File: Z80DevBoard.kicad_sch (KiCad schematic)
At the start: 163 parts, among them J1 Conn_01x02_Pin, J2 Conn_02x20_Top_Bottom, J3 Conn_02x10_Top_Bottom, SW1 WAIT, SW2 RESET, SW3 Z80BOOT, SW4 RPBOOT, SW5 SW_Nidec_CAS-120A1, SW6 Z80_CLOCK, U1 74HC14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

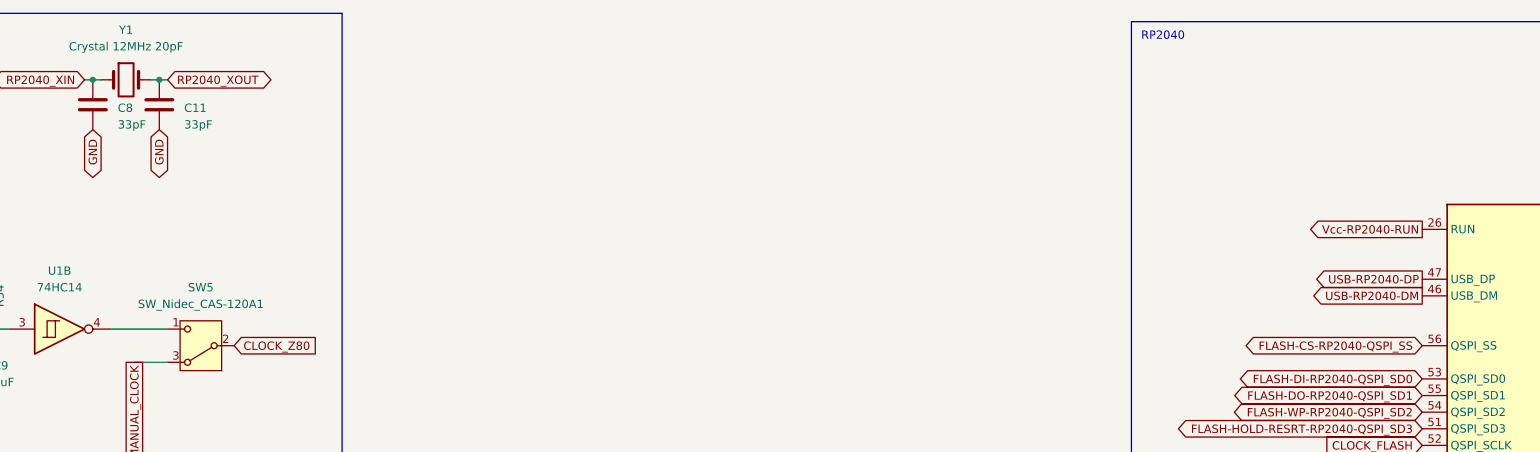
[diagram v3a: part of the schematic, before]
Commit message: Fixed the RP2040 clock capacitors. Added 2 resistors to the RP2040's XIN-XOUT.
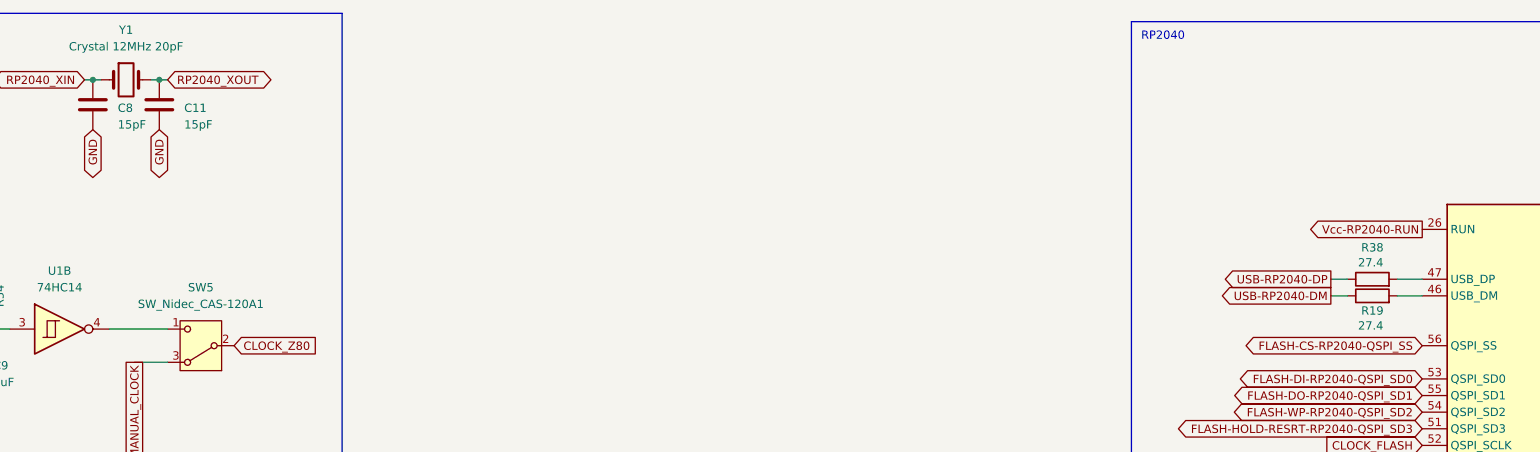
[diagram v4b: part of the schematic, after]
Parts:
- added R19, R38: 27.4, Resistor_THT:R_Axial_DIN0207_L6.3mm_D2.5mm_P10.16mm_Horizontal, symbol Device:R
- C11, C8: value 33pF -> 15pF
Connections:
- net USB-RP2040-DM: now also R19.1; no longer RP2040_1.46 (USB_DM)
- net USB-RP2040-DP: now also R38.1; no longer RP2040_1.47 (USB_DP)
- new net: R19.2, RP2040_1.46 (USB_DM)
- new net: R38.2, RP2040_1.47 (USB_DP)
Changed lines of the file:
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@@
 	(title_block
 		(title "Z80DevBoard")
-		(date "2026-03-12")
+		(date "2026-03-24")
 		(company "Gianluca Rainis")
 		(comment 1 "gianluca-rainis on GitHub")
@@
 	(wire
 		(pts
+			(xy 311.15 58.42) (xy 314.96 58.42)
+		)
+		(stroke
+			(width 0)
+			(type default)
+		)
+	)
+	(wire
+		(pts
 			(xy 458.47 43.18) (xy 452.12 43.18)
 		)
@@
 	(wire
 		(pts
+			(xy 311.15 55.88) (xy 314.96 55.88)
+		)
+		(stroke
+			(width 0)
+			(type default)
+		)
+	)
+	(wire
+		(pts
 			(xy 46.99 378.46) (xy 46.99 382.27)
 		)
@@
 	(wire
 		(pts
+			(xy 300.99 55.88) (xy 303.53 55.88)
+		)
+		(stroke
+			(width 0)
+			(type default)
+		)
+	)
+	(wire
+		(pts
 			(xy 466.09 193.04) (xy 490.22 193.04)
 		)
@@
 	(wire
 		(pts
+			(xy 300.99 58.42) (xy 303.53 58.42)
+		)
+		(stroke
+			(width 0)
+			(type default)
+		)
+	)
+	(wire
+		(pts
 			(xy 524.51 187.96) (xy 537.21 187.96)
 		)
@@
 	(global_label "USB-RP2040-DM"
 		(shape output)
-		(at 314.96 58.42 180)
+		(at 300.99 58.42 180)
 		(fields_autoplaced yes)
 		(effects
@@
 		)
 		(property "Intersheetrefs" "${INTERSHEET_REFS}"
-			(at 294.9206 58.42 0)
+			(at 280.9506 58.42 0)
 			(effects
 				(font
@@
 	(global_label "USB-RP2040-DP"
 		(shape output)
-		(at 314.96 55.88 180)
+		(at 300.99 55.88 180)
 		(fields_autoplaced yes)
 		(effects
@@
 		)
 		(property "Intersheetrefs" "${INTERSHEET_REFS}"
-			(at 295.102 55.88 0)
+			(at 281.132 55.88 0)
 			(effects
 				(font
@@
 			)
 		)
-		(property "Value" "33pF"
+		(property "Value" "15pF"
 			(at 115.57 32.258 0)
 			(effects
@@
 	)
 	(symbol
+		(lib_id "Device:R")
+		(at 307.34 58.42 90)
+		(unit 1)
+		(exclude_from_sim no)
+		(in_bom yes)
+		(on_board yes)
+		(dnp no)
+		(property "Reference" "R19"
+			(at 307.34 60.706 90)
+			(effects
+				(font
+					(size 1.27 1.27)
+				)
+			)
+		)
+		(property "Value" "27.4"
+			(at 307.086 62.992 90)
+			(effects
+				(font
+					(size 1.27 1.27)
+				)
+			)
+		)
+		(property "Footprint" "Resistor_THT:R_Axial_DIN0207_L6.3mm_D2.5mm_P10.16mm_Horizontal"
+			(at 307.34 60.198 90)
+			(effects
+				(font
+					(size 1.27 1.27)
+				)
+				(hide yes)
+			)
+		)
+		(property "Datasheet" "~"
+			(at 307.34 58.42 0)
+			(effects
+				(font
+					(size 1.27 1.27)
+				)
+				(hide yes)
+			)
+		)
+		(property "Description" "Resistor"
+			(at 307.34 58.42 0)
+			(effects
+				(font
+					(size 1.27 1.27)
+				)
+				(hide yes)
+			)
+		)
+		(pin "1"
+		)
+		(pin "2"
+		)
+		(instances
+			(project "Z80DevBoard"
+				(path "/e1d3a7c4-9081-48b0-8f4d-5da429793ec4"
+					(reference "R19")
+					(unit 1)
+				)
+			)
+		)
+	)
+	(symbol
 		(lib_id "Device:LED")
 		(at 110.49 335.28 0)
@@
 			)
 		)
-		(property "Value" "33pF"
+		(property "Value" "15pF"
 			(at 125.73 32.258 0)
 			(effects
@@
 					(unit 1)
 				)
+			)
+		)
+	)
+	(symbol
+		(lib_id "Device:R")
+		(at 307.34 55.88 90)
+		(unit 1)
+		(exclude_from_sim no)
+		(in_bom yes)
+		(on_board yes)
+		(dnp no)
+		(property "Reference" "R38"
+			(at 307.34 51.054 90)
+			(effects
+				(font
+					(size 1.27 1.27)
+				)
+			)
+		)
+		(property "Value" "27.4"
+			(at 307.086 53.34 90)
+			(effects
+				(font
+					(size 1.27 1.27)
+				)
+			)
+		)
+		(property "Footprint" "Resistor_THT:R_Axial_DIN0207_L6.3mm_D2.5mm_P10.16mm_Horizontal"
+			(at 307.34 57.658 90)
+			(effects
+				(font
+					(size 1.27 1.27)
+				)
+				(hide yes)
+			)
+		)
+		(property "Datasheet" "~"
+			(at 307.34 55.88 0)
+			(effects
+				(font
+					(size 1.27 1.27)
+				)
+				(hide yes)
+			)
+		)
+		(property "Description" "Resistor"
+			(at 307.34 55.88 0)
+			(effects
+				(font
+					(size 1.27 1.27)
+				)
+				(hide yes)
+			)
+		)
+		(pin "1"
+		)
+		(pin "2"
+		)
+		(instances
+			(project "Z80DevBoard"
+				(path "/e1d3a7c4-9081-48b0-8f4d-5da429793ec4"
+					(reference "R38")
+					(unit 1)
+				)

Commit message: Fixed some resistors.
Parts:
- R10, R11, R20, R21, R4, R7, R8, R9: value 220 -> 1k
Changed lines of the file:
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@@
 	(title_block
 		(title "Z80DevBoard")
-		(date "2026-03-24")
+		(date "2026-03-25")
 		(company "Gianluca Rainis")
 		(comment 1 "gianluca-rainis on GitHub")
@@
 			)
 		)
-		(property "Value" "220"
+		(property "Value" "1k"
 			(at 91.44 332.7399 0)
 			(effects
@@
 			)
 		)
-		(property "Value" "220"
+		(property "Value" "1k"
 			(at 66.04 332.7399 0)
 			(effects
@@
 			)
 		)
-		(property "Value" "220"
+		(property "Value" "1k"
 			(at 43.18 332.7399 0)
 			(effects
@@
 			)
 		)
-		(property "Value" "220"
+		(property "Value" "1k"
 			(at 116.84 332.7399 0)
 			(effects
@@
 			)
 		)
-		(property "Value" "220"
+		(property "Value" "1k"
 			(at 298.45 269.24 90)
 			(effects
@@
 			)
 		)
-		(property "Value" "220"
+		(property "Value" "1k"
 			(at 298.45 280.67 90)
 			(effects
@@
 			)
 		)
-		(property "Value" "220"
+		(property "Value" "1k"
 			(at 142.24 332.7399 0)
 			(effects
@@
 			)
 		)
-		(property "Value" "220"
+		(property "Value" "1k"
 			(at 167.64 332.7399 0)
 			(effects

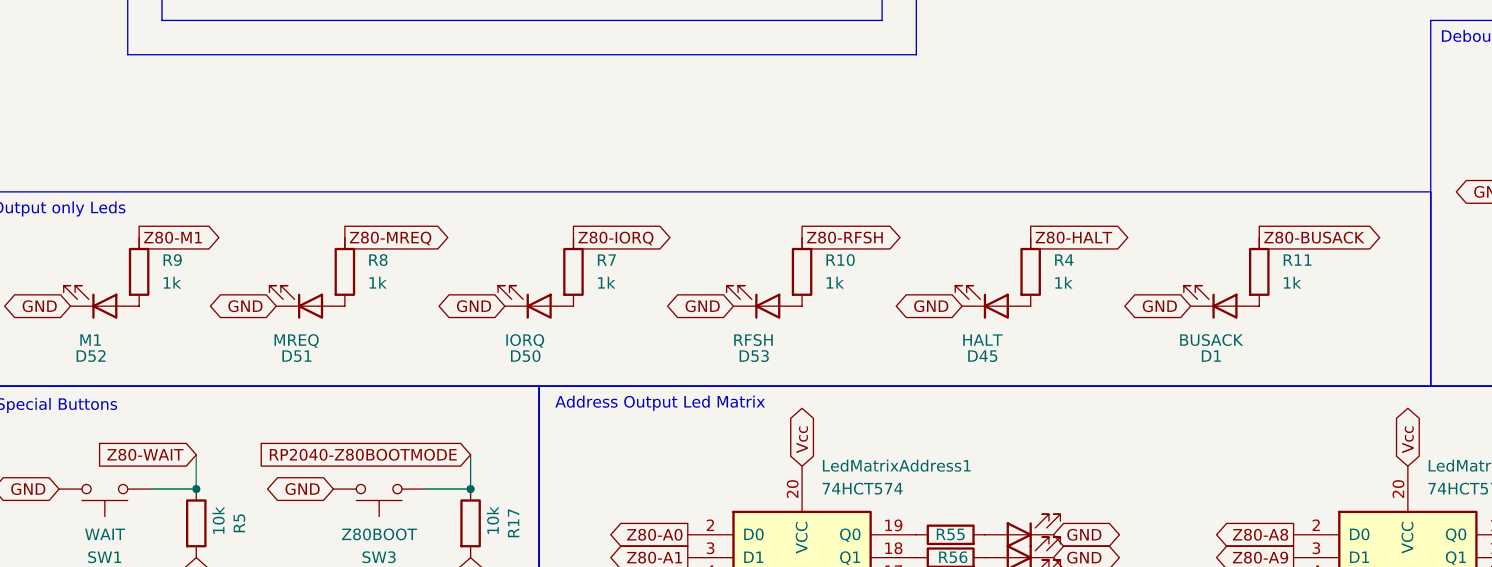
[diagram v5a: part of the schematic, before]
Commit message: Fixed some connections. Fixed some resistors values.
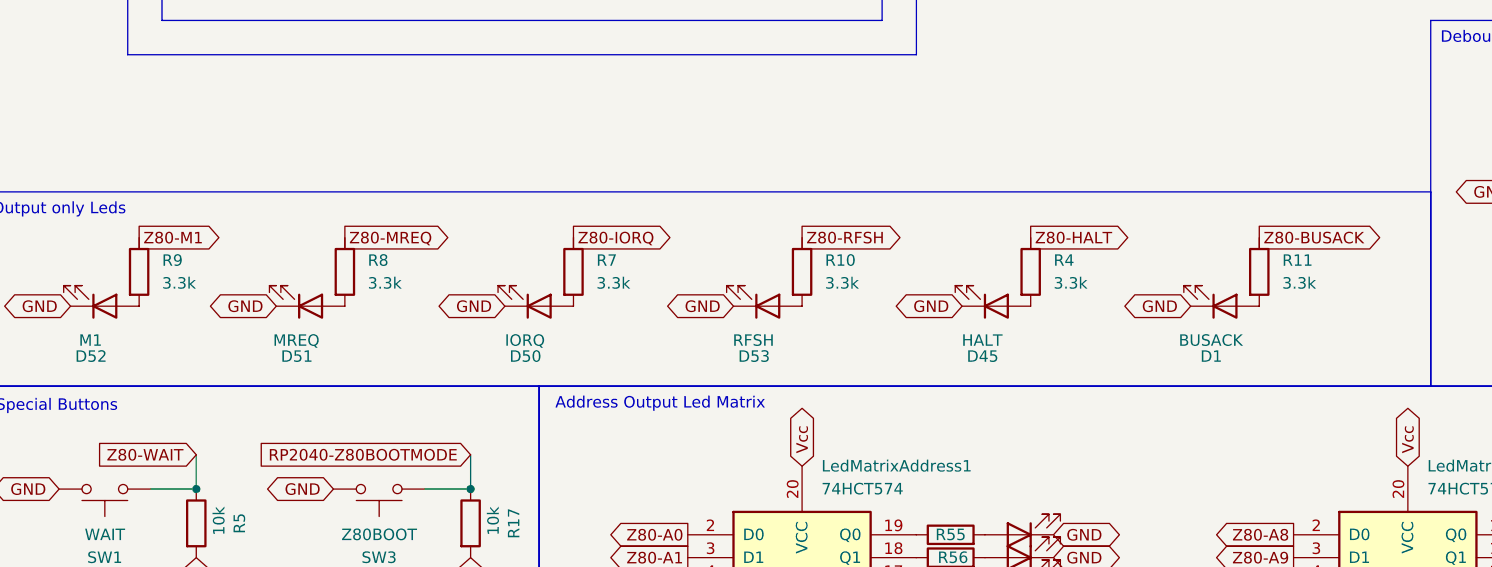
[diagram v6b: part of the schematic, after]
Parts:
- R10, R11, R4, R7, R8, R9: value 1k -> 3.3k
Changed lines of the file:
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@@
 			)
 		)
-		(property "Value" "1k"
+		(property "Value" "3.3k"
 			(at 91.44 332.7399 0)
 			(effects
@@
 			)
 		)
-		(property "Value" "1k"
+		(property "Value" "3.3k"
 			(at 66.04 332.7399 0)
 			(effects
@@
 			)
 		)
-		(property "Value" "1k"
+		(property "Value" "3.3k"
 			(at 43.18 332.7399 0)
 			(effects
@@
 			)
 		)
-		(property "Value" "1k"
+		(property "Value" "3.3k"
 			(at 116.84 332.7399 0)
 			(effects
@@
 			)
 		)
-		(property "Value" "1k"
+		(property "Value" "3.3k"
 			(at 142.24 332.7399 0)
 			(effects
@@
 			)
 		)
-		(property "Value" "1k"
+		(property "Value" "3.3k"
 			(at 167.64 332.7399 0)
 			(effects

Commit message: Added the debauncers for the Reset and the Wait buttons. Added a TXS0102DCT for the busack and busreq connections between the Z80 and the RP2040.
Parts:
- added C12, C14: 0.1uF, Capacitor_THT:CP_Radial_D4.0mm_P1.50mm, symbol Device:C
- added R39, R40: 10k, Resistor_THT:R_Axial_DIN0207_L6.3mm_D2.5mm_P10.16mm_Horizontal, symbol Device:R
- added unit 3 of U1
- added unit 4 of U1
- added U6: TXS0102DCT, Package_SO:SSOP-8_2.95x2.8mm_P0.65mm, symbol Logic_LevelTranslator:TXS0102DCT
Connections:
- net GND: now also C12.1, C14.1, U6.2 (GND)
- net RP2040-GPIO12: now also J3.1 (Pin_1); no longer J3.3 (Pin_3)
- net RP2040-GPIO13: now also J3.2 (Pin_2); no longer J3.4 (Pin_4)
- net RP2040-GPIO14: now also J3.3 (Pin_3); no longer J3.5 (Pin_5)
- net RP2040-GPIO15: now also J3.4 (Pin_4); no longer J3.6 (Pin_6)
- net RP2040-GPIO16: now also J3.5 (Pin_5); no longer J3.7 (Pin_7)
- net RP2040-GPIO17: now also J3.6 (Pin_6); no longer J3.8 (Pin_8)
- net RP2040-GPIO18: now also J3.7 (Pin_7); no longer J3.9 (Pin_9)
- net RP2040-GPIO19: now also J3.8 (Pin_8); no longer J3.10 (Pin_10)
- net RP2040-GPIO20: now also J3.9 (Pin_9); no longer J3.11 (Pin_11)
- net RP2040-GPIO21: now also J3.10 (Pin_10); no longer J3.12 (Pin_12)
- net RP2040-GPIO22: now also J3.11 (Pin_11); no longer J3.13 (Pin_13)
- net RP2040-GPIO23: now also J3.12 (Pin_12); no longer J3.14 (Pin_14)
- net RP2040-GPIO24: now also J3.13 (Pin_13); no longer J3.15 (Pin_15)
- net RP2040-GPIO25: now also J3.14 (Pin_14); no longer J3.16 (Pin_16)
- net RP2040-GPIO26-ADC0: now also J3.15 (Pin_15); no longer J3.17 (Pin_17)
- net RP2040-GPIO27-ADC1: now also J3.16 (Pin_16); no longer J3.18 (Pin_18)
- net Vcc: now also U6.7 (VCCB)
- net Vdd_3v3: now also U6.3 (VCCA), U6.6 (OE)
- net Z80-BUSACK: now also U6.1 (B2)
- net Z80-BUSREQ: now also U6.8 (B1)
- net Z80-RESET: now also U1.8; no longer R6.1, SW2.2
- net Z80-WAIT: now also U1.6; no longer R5.1, SW1.2
- net RP2040-GPIO28-ADC2: now reaches RP2040_1.40 (GPIO28_ADC2)
- net RP2040-GPIO28-ADC2: now also J3.17 (Pin_17)
- net RP2040-GPIO29-ADC3: now reaches RP2040_1.41 (GPIO29_ADC3)
- net RP2040-GPIO29-ADC3: now also J3.18 (Pin_18)
- net RP2040-GPIO10 renamed RP2040-GPIO10-BUSREQ
- net RP2040-GPIO10-BUSREQ: now also U6.5 (A1); no longer J3.1 (Pin_1)
- net RP2040-GPIO11 renamed RP2040-GPIO11-BUSACK
- net RP2040-GPIO11-BUSACK: now also U6.4 (A2); no longer J3.2 (Pin_2)
- new net: C12.2, R39.2, U1.5
- new net: R39.1, R5.1, SW1.2
- new net: R40.1, R6.1, SW2.2
- new net: C14.2, R40.2, U1.9
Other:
- note added: "RP2040 Z80 Connections"
- moved on the sheet: C7, Flash1, R17, R18, R5, R6, RAM1, RAM2, SW1, SW2, SW3, SW4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

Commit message: Fixed the capacitors sizes.
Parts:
- C1, C10, C11, C12, C13, C14, C2, C3, C4, C5, C6, C7, C8, C9: footprint Capacitor_THT:CP_Radial_D4.0mm_P1.50mm -> Capacitor_THT:CP_Radial_D4.0mm_P2.00mm
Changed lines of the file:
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@@
 			)
 		)
-		(property "Footprint" "Capacitor_THT:CP_Radial_D4.0mm_P1.50mm"
+		(property "Footprint" "Capacitor_THT:CP_Radial_D4.0mm_P2.00mm"
 			(at 221.2848 287.02 0)
 			(effects
@@
 			)
 		)
-		(property "Footprint" "Capacitor_THT:CP_Radial_D4.0mm_P1.50mm"
+		(property "Footprint" "Capacitor_THT:CP_Radial_D4.0mm_P2.00mm"
 			(at 110.7948 25.4 0)
 			(effects
@@
 			)
 		)
-		(property "Footprint" "Capacitor_THT:CP_Radial_D4.0mm_P1.50mm"
+		(property "Footprint" "Capacitor_THT:CP_Radial_D4.0mm_P2.00mm"
 			(at 20.6248 72.39 0)
 			(effects
@@
 			)
 		)
-		(property "Footprint" "Capacitor_THT:CP_Radial_D4.0mm_P1.50mm"
+		(property "Footprint" "Capacitor_THT:CP_Radial_D4.0mm_P2.00mm"
 			(at 43.4848 31.75 0)
 			(effects
@@
 			)
 		)
-		(property "Footprint" "Capacitor_THT:CP_Radial_D4.0mm_P1.50mm"
+		(property "Footprint" "Capacitor_THT:CP_Radial_D4.0mm_P2.00mm"
 			(at 80.3148 261.62 0)
 			(effects
@@
 			)
 		)
-		(property "Footprint" "Capacitor_THT:CP_Radial_D4.0mm_P1.50mm"
+		(property "Footprint" "Capacitor_THT:CP_Radial_D4.0mm_P2.00mm"
 			(at 71.4248 72.39 0)
 			(effects
@@
 			)
 		)
-		(property "Footprint" "Capacitor_THT:CP_Radial_D4.0mm_P1.50mm"
+		(property "Footprint" "Capacitor_THT:CP_Radial_D4.0mm_P2.00mm"
 			(at 66.3448 31.75 0)
 			(effects
@@
 			)
 		)
-		(property "Footprint" "Capacitor_THT:CP_Radial_D4.0mm_P1.50mm"
+		(property "Footprint" "Capacitor_THT:CP_Radial_D4.0mm_P2.00mm"
 			(at 218.7448 322.58 0)
 			(effects
@@
 			)
 		)
-		(property "Footprint" "Capacitor_THT:CP_Radial_D4.0mm_P1.50mm"
+		(property "Footprint" "Capacitor_THT:CP_Radial_D4.0mm_P2.00mm"
 			(at 91.7448 64.77 0)
 			(effects
@@
 			)
 		)
-		(property "Footprint" "Capacitor_THT:CP_Radial_D4.0mm_P1.50mm"
+		(property "Footprint" "Capacitor_THT:CP_Radial_D4.0mm_P2.00mm"
 			(at 221.2848 252.73 0)
 			(effects
@@
 			)
 		)
-		(property "Footprint" "Capacitor_THT:CP_Radial_D4.0mm_P1.50mm"
+		(property "Footprint" "Capacitor_THT:CP_Radial_D4.0mm_P2.00mm"
 			(at 32.0548 72.39 0)
 			(effects
@@
 			)
 		)
-		(property "Footprint" "Capacitor_THT:CP_Radial_D4.0mm_P1.50mm"
+		(property "Footprint" "Capacitor_THT:CP_Radial_D4.0mm_P2.00mm"
 			(at 44.7548 72.39 0)
 			(effects
@@
 			)
 		)
-		(property "Footprint" "Capacitor_THT:CP_Radial_D4.0mm_P1.50mm"
+		(property "Footprint" "Capacitor_THT:CP_Radial_D4.0mm_P2.00mm"
 			(at 57.4548 72.39 0)
 			(effects
@@
 			)
 		)
-		(property "Footprint" "Capacitor_THT:CP_Radial_D4.0mm_P1.50mm"
+		(property "Footprint" "Capacitor_THT:CP_Radial_D4.0mm_P2.00mm"
 			(at 120.9548 25.4 0)
 			(effects
